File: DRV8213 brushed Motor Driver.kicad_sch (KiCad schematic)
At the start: 26 parts, among them J1 Keystone 6102, J10 Precidip 852-10-004-20-001101, J11 Precidip 852-10-004-20-001101, J2 Keystone 6102, J3 Keystone 6100, J4 Keystone 6100, J5 Keystone 6102, J6 Keystone 6102, J7 Keystone 6100, J8 Keystone 6100, J9 JST PH 2mm horizontal, U1 DRV8213RTER, U2 LP2981-3.3

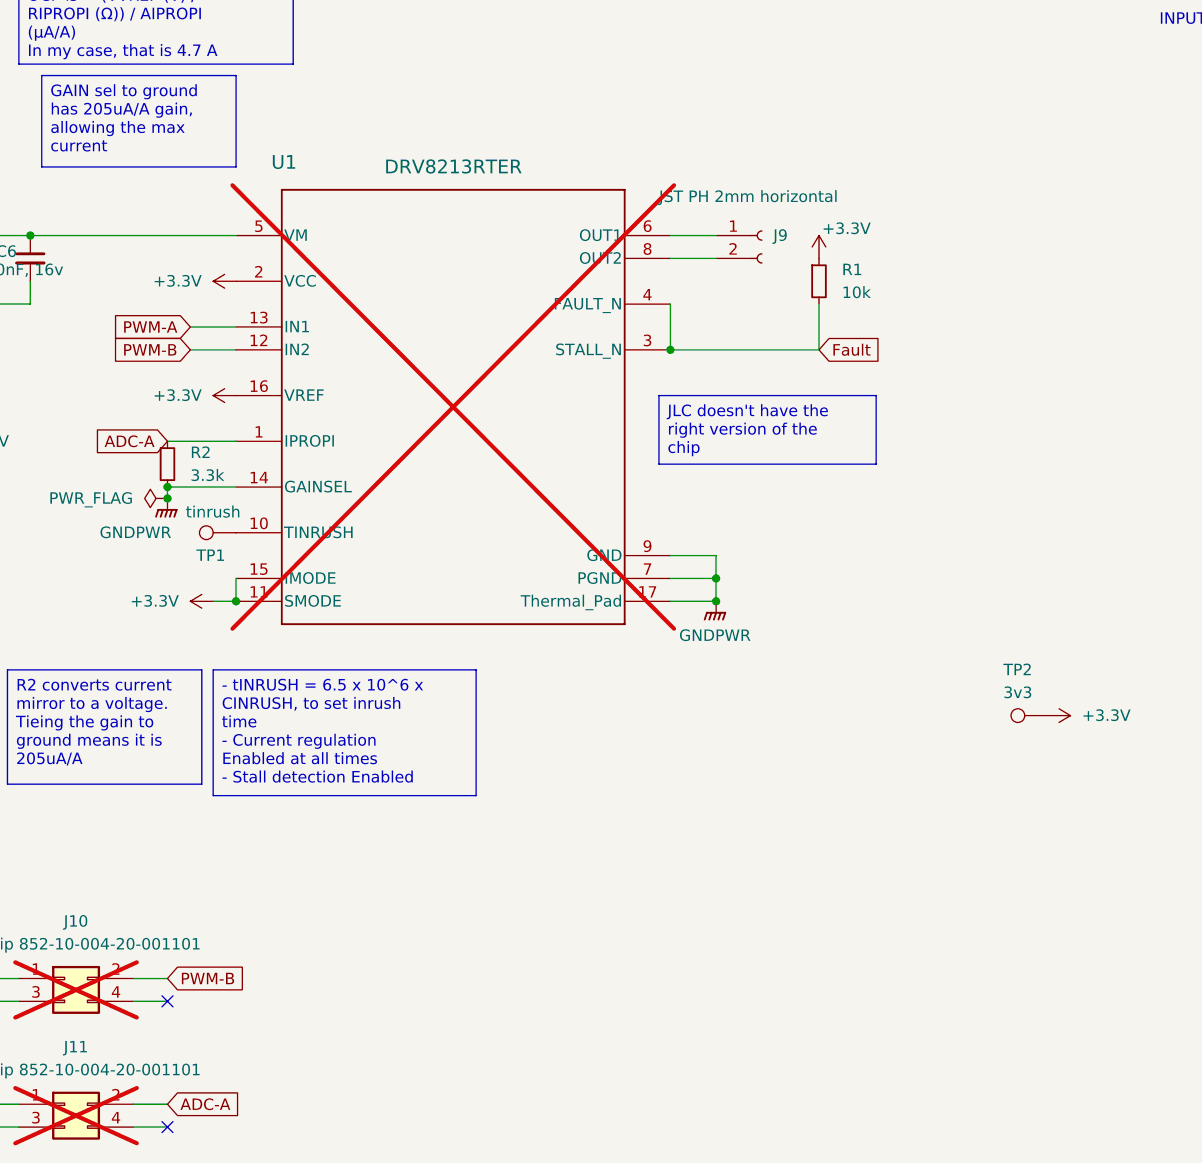
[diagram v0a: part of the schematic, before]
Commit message: Split Stall and Fault detection
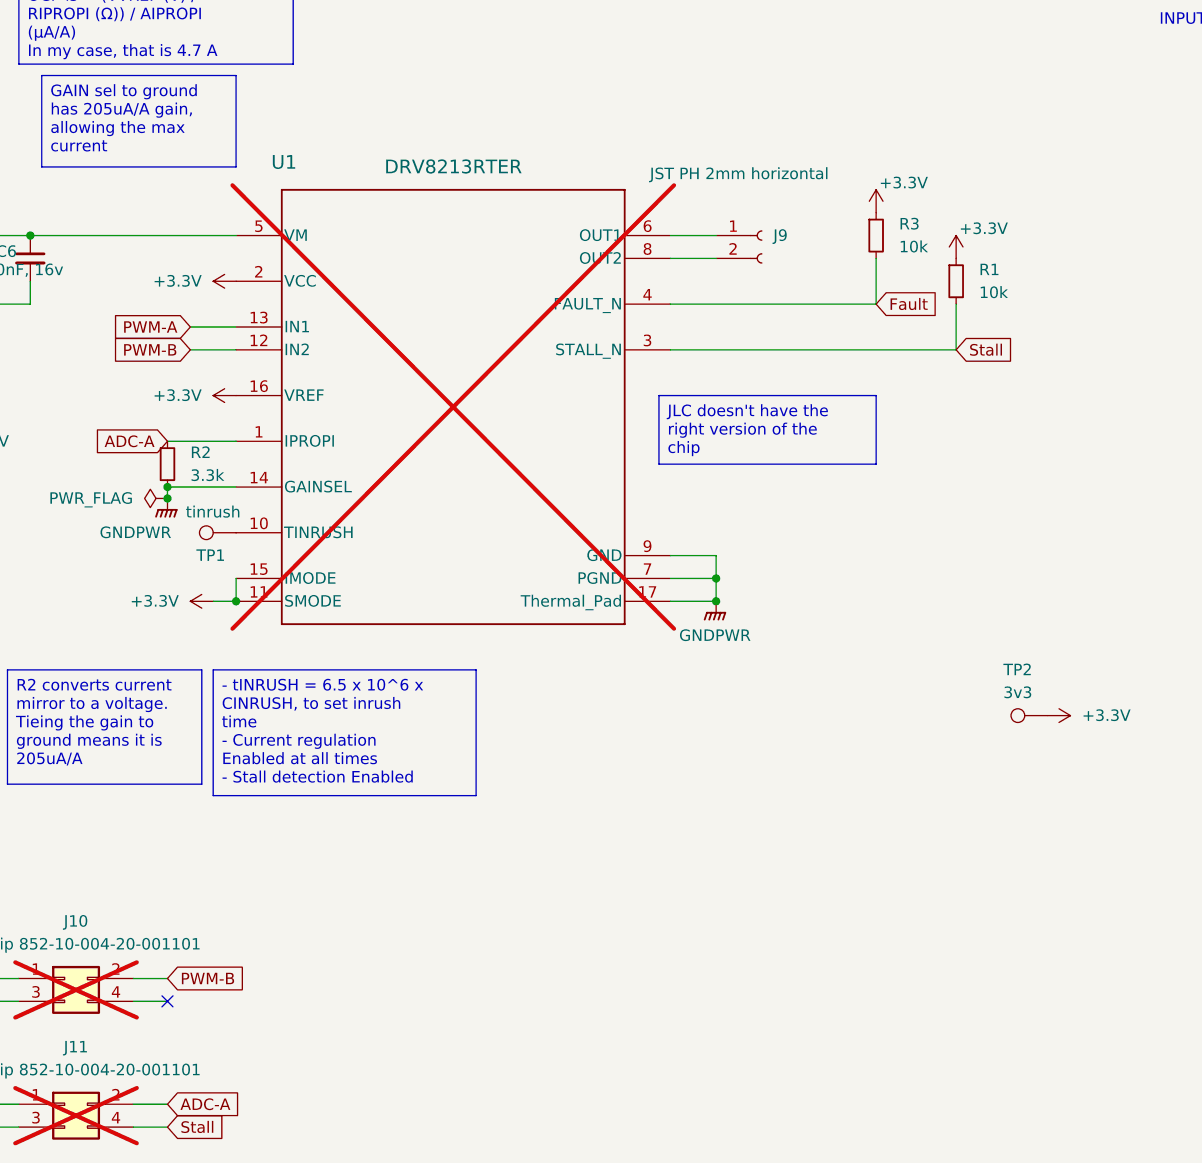
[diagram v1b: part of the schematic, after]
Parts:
- added R3: 10k, Resistor_SMD:R_0402_1005Metric, symbol Device:R_Small
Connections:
- net +3.3V: now also R3.1
- net Fault: now also R3.2; no longer R1.2, U1.3 (STALL_N)
- net Stall: now reaches J11.4 (Pin_4)
- net Stall: now also R1.2, U1.3 (STALL_N)
- no-connect marks 4 -> 3
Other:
- moved on the sheet: R1
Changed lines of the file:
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@@
 		(color 0 0 0 0)
 	)
-	(junction
-		(at 135.89 72.39)
-		(diameter 0)
-		(color 0 0 0 0)
-	)
 	(no_connect
 		(at 52.07 91.44)
 	)
 	(no_connect
-		(at 80.01 158.75)
-	)
-	(no_connect
 		(at 59.69 144.78)
 	)
@@
 	(wire
 		(pts
+			(xy 135.89 72.39) (xy 167.64 72.39)
+		)
+		(stroke
+			(width 0)
+			(type default)
+		)
+	)
+	(wire
+		(pts
 			(xy 215.9 43.18) (xy 215.9 46.99)
 		)
@@
 	(wire
 		(pts
+			(xy 158.75 62.23) (xy 158.75 67.31)
+		)
+		(stroke
+			(width 0)
+			(type default)
+		)
+	)
+	(wire
+		(pts
 			(xy 80.01 142.24) (xy 76.2 142.24)
 		)
@@
 	(wire
 		(pts
-			(xy 152.4 72.39) (xy 135.89 72.39)
+			(xy 135.89 67.31) (xy 158.75 67.31)
 		)
 		(stroke
@@
 	(wire
 		(pts
-			(xy 152.4 67.31) (xy 152.4 72.39)
+			(xy 167.64 67.31) (xy 167.64 72.39)
 		)
 		(stroke
@@
 	(wire
 		(pts
-			(xy 135.89 67.31) (xy 135.89 72.39)
-		)
-		(stroke
-			(width 0)
-			(type default)
-		)
-	)
-	(wire
-		(pts
 			(xy 80.01 87.63) (xy 80.01 88.9)
 		)
@@
 		)
 	)
-	(global_label "Fault"
+	(global_label "Stall"
 		(shape input)
-		(at 152.4 72.39 0)
+		(at 167.64 72.39 0)
 		(fields_autoplaced yes)
 		(effects
@@
 		)
 		(property "Intersheetrefs" "${INTERSHEET_REFS}"
-			(at 160.1627 72.39 0)
+			(at 175.0398 72.39 0)
 			(effects
 				(font
@@
 		)
 	)
+	(global_label "Stall"
+		(shape input)
+		(at 80.01 158.75 0)
+		(fields_autoplaced yes)
+		(effects
+			(font
+				(size 1.27 1.27)
+			)
+			(justify left)
+		)
+		(property "Intersheetrefs" "${INTERSHEET_REFS}"
+			(at 87.4098 158.75 0)
+			(effects
+				(font
+					(size 1.27 1.27)
+				)
+				(justify left)
+				(hide yes)
+			)
+		)
+	)
 	(global_label "ADC-A"
 		(shape input)
@@
 	(global_label "Fault"
 		(shape input)
+		(at 158.75 67.31 0)
+		(fields_autoplaced yes)
+		(effects
+			(font
+				(size 1.27 1.27)
+			)
+			(justify left)
+		)
+		(property "Intersheetrefs" "${INTERSHEET_REFS}"
+			(at 166.5127 67.31 0)
+			(effects
+				(font
+					(size 1.27 1.27)
+				)
+				(justify left)
+				(hide yes)
+			)
+		)
+	)
+	(global_label "Fault"
+		(shape input)
 		(at 59.69 158.75 180)
 		(fields_autoplaced yes)
@@
 	)
 	(symbol
+		(lib_id "Device:R_Small")
+		(at 158.75 59.69 0)
+		(unit 1)
+		(exclude_from_sim no)
+		(in_bom yes)
+		(on_board yes)
+		(dnp no)
+		(fields_autoplaced yes)
+		(property "Reference" "R3"
+			(at 161.29 58.4199 0)
+			(effects
+				(font
+					(size 1.27 1.27)
+				)
+				(justify left)
+			)
+		)
+		(property "Value" "10k"
+			(at 161.29 60.9599 0)
+			(effects
+				(font
+					(size 1.27 1.27)
+				)
+				(justify left)
+			)
+		)
+		(property "Footprint" "Resistor_SMD:R_0402_1005Metric"
+			(at 158.75 59.69 0)
+			(effects
+				(font
+					(size 1.27 1.27)
+				)
+				(hide yes)
+			)
+		)
+		(property "Datasheet" "~"
+			(at 158.75 59.69 0)
+			(effects
+				(font
+					(size 1.27 1.27)
+				)
+				(hide yes)
+			)
+		)
+		(property "Description" "Resistor, small symbol"
+			(at 158.75 59.69 0)
+			(effects
+				(font
+					(size 1.27 1.27)
+				)
+				(hide yes)
+			)
+		)
+		(property "LCSC" "C25744"
+			(at 161.29 58.4199 0)
+			(effects
+				(font
+					(size 1.27 1.27)
+				)
+				(hide yes)
+			)
+		)
+		(pin "2"
+		)
+		(pin "1"
+		)
+		(instances
+			(project "DRV8213 brushed Motor Driver"
+				(path "/8760dbe3-976e-4366-afd9-aec15b99495c"
+					(reference "R3")
+					(unit 1)
+				)
+			)
+		)
+	)
+	(symbol
 		(lib_id "Connector:Conn_01x01_Pin")
 		(at 209.55 43.18 0)
@@
 	)
 	(symbol
+		(lib_id "power:+3.3V")
+		(at 158.75 57.15 0)
+		(unit 1)
+		(exclude_from_sim no)
+		(in_bom yes)
+		(on_board yes)
+		(dnp no)
+		(property "Reference" "#PWR017"
+			(at 158.75 60.96 0)
+			(effects
+				(font
+					(size 1.27 1.27)
+				)
+				(hide yes)
+			)
+		)
+		(property "Value" "+3.3V"
+			(at 161.798 53.848 0)
+			(effects
+				(font
+					(size 1.27 1.27)
+				)
+			)
+		)
+		(property "Footprint" ""
+			(at 158.75 57.15 0)
+			(effects
+				(font
+					(size 1.27 1.27)
+				)
+				(hide yes)
+			)
+		)
+		(property "Datasheet" ""
+			(at 158.75 57.15 0)
+			(effects
+				(font
+					(size 1.27 1.27)
+				)
+				(hide yes)
+			)
+		)
+		(property "Description" "Power symbol creates a global label with name \"+3.3V\""
+			(at 158.75 57.15 0)
+			(effects
+				(font
+					(size 1.27 1.27)
+				)
+				(hide yes)
+			)
+		)
+		(pin "1"
+		)
+		(instances
+			(project "DRV8213 brushed Motor Driver"
+				(path "/8760dbe3-976e-4366-afd9-aec15b99495c"
+					(reference "#PWR017")
+					(unit 1)
+				)
+			)
+		)
+	)
+	(symbol
 		(lib_id "power:VDD")
 		(at 21.59 59.69 90)
@@
 	(symbol
 		(lib_id "power:+3.3V")
-		(at 152.4 62.23 0)
+		(at 167.64 62.23 0)
 		(unit 1)
 		(exclude_from_sim no)
@@
 		(dnp no)
 		(property "Reference" "#PWR06"
-			(at 152.4 66.04 0)
+			(at 167.64 66.04 0)
 			(effects
 				(font
@@
 		)
 		(property "Value" "+3.3V"
-			(at 155.448 58.928 0)
+			(at 170.688 58.928 0)
 			(effects
 				(font
@@
 		)
 		(property "Footprint" ""
-			(at 152.4 62.23 0)
+			(at 167.64 62.23 0)
 			(effects
 				(font
@@
 		)
 		(property "Datasheet" ""
-			(at 152.4 62.23 0)
+			(at 167.64 62.23 0)
 			(effects
 				(font
@@
 		)
 		(property "Description" "Power symbol creates a global label with name \"+3.3V\""
-			(at 152.4 62.23 0)
+			(at 167.64 62.23 0)
 			(effects
 				(font
@@
 		)
 		(property "Value" "JST PH 2mm horizontal"
-			(at 134.62 55.372 0)
+			(at 133.604 52.832 0)
 			(effects
 				(font
@@
 	(symbol
 		(lib_id "Device:R_Small")
-		(at 152.4 64.77 0)
+		(at 167.64 64.77 0)
 		(unit 1)
 		(exclude_from_sim no)
@@
 		(fields_autoplaced yes)
 		(property "Reference" "R1"
-			(at 154.94 63.4999 0)
+			(at 170.18 63.4999 0)
 			(effects
 				(font
@@
 		)
 		(property "Value" "10k"
-			(at 154.94 66.0399 0)
+			(at 170.18 66.0399 0)
 			(effects
 				(font
@@
 		)
 		(property "Footprint" "Resistor_SMD:R_0402_1005Metric"
-			(at 152.4 64.77 0)
+			(at 167.64 64.77 0)
 			(effects
 				(font
@@
 		)
 		(property "Datasheet" "~"
-			(at 152.4 64.77 0)
+			(at 167.64 64.77 0)
 			(effects
 				(font
@@
 		)
 		(property "Description" "Resistor, small symbol"
-			(at 152.4 64.77 0)
+			(at 167.64 64.77 0)
 			(effects
 				(font
@@
 		)
 		(property "LCSC" "C25744"
-			(at 154.94 63.4999 0)
+			(at 170.18 63.4999 0)
 			(effects
 				(font

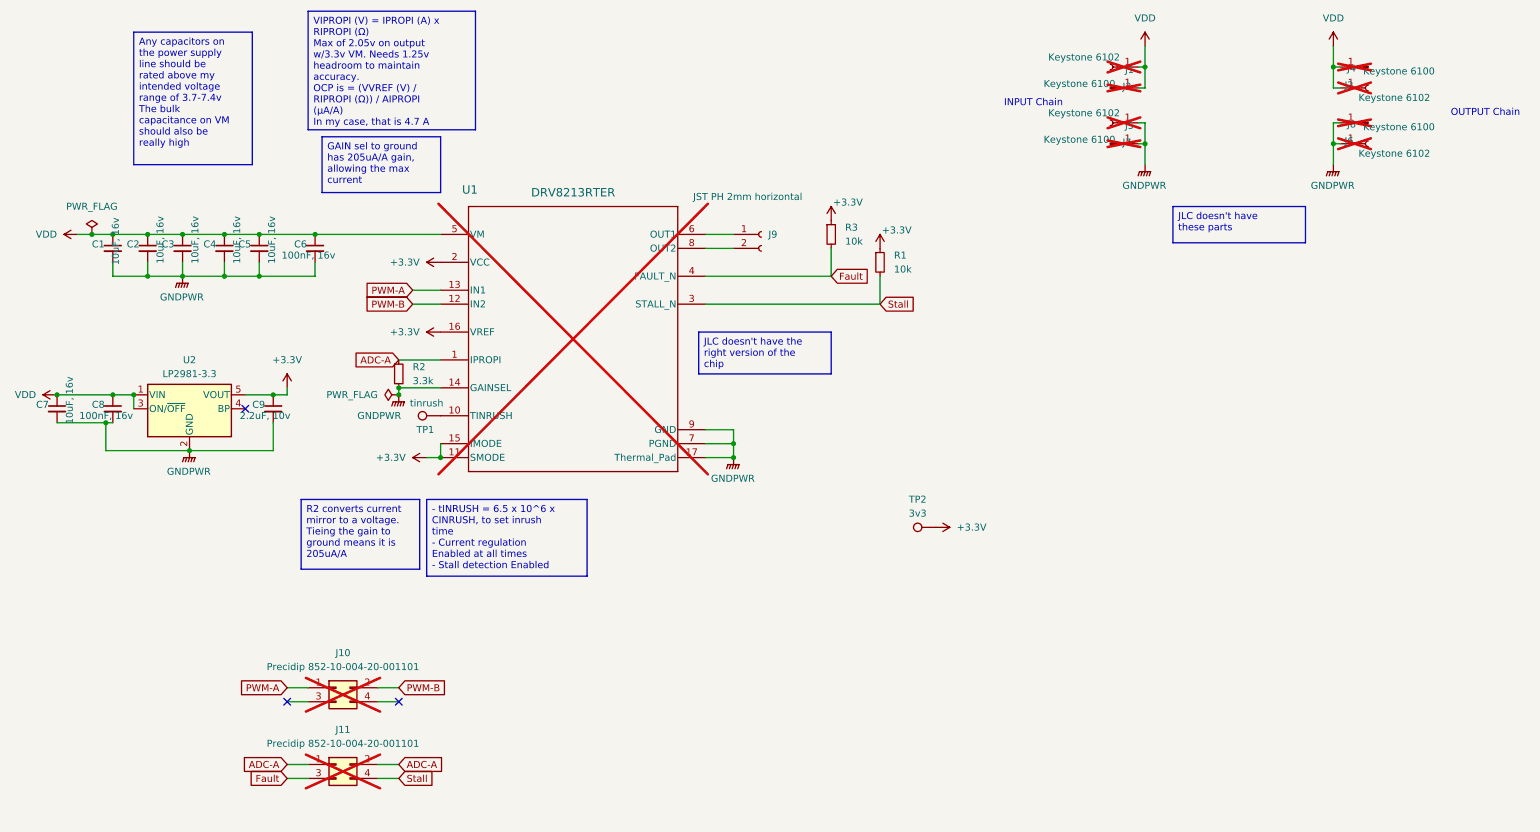
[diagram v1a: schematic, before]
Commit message: Clarified 3v3 regulator and caps
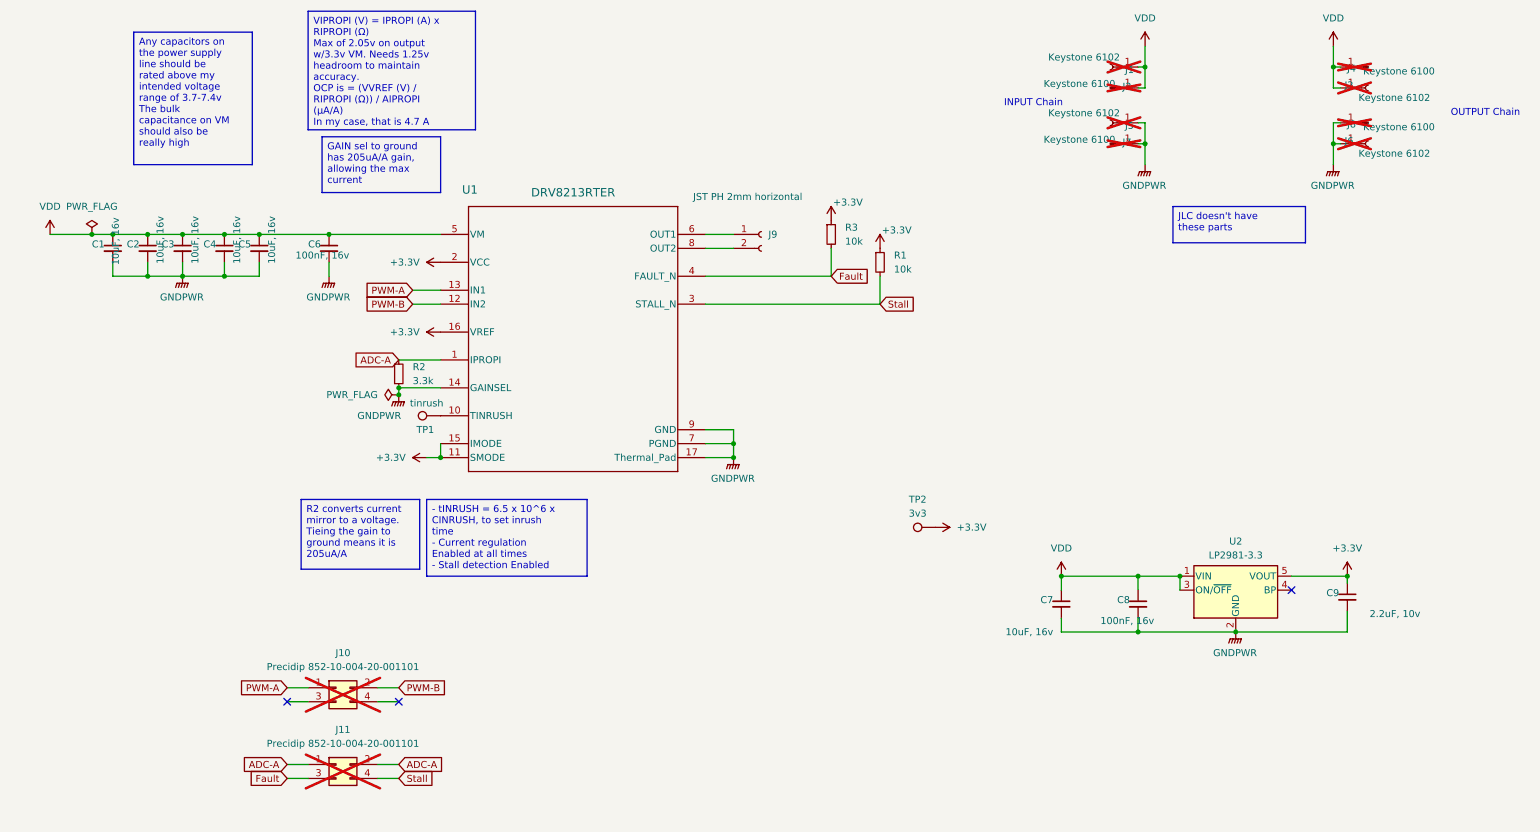
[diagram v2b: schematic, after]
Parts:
- U1: now fitted
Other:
- moved on the sheet: C6, C7, C8, C9, U2
